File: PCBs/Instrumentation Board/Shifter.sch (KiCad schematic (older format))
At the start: 3 parts, among them U8 PI4ULS5V201TAEX

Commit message: Started instrumentation Netlist
Finished footprints for shifter, regulators and IMUs
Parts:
- U8: footprint (none) -> sot:SOT-23-6; symbol PI4ULS5V201TAEX -> PI4ULS5V201TAEX-RESCUE-instrumentation_board
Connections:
- no-connect marks 2 -> 0
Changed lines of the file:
@@
 EESchema Schematic File Version 2
+LIBS:instrumentation_board-rescue
 LIBS:power
 LIBS:device
@@
 $Descr A4 11693 8268
 encoding utf-8
-Sheet 5 10
+Sheet 7 10
 Title ""
 Date ""
@@
 $EndDescr
 $Comp
-L PI4ULS5V201TAEX U8
+L PI4ULS5V201TAEX-RESCUE-instrumentation_board U8
 U 1 1 5AB871B5
 P 5050 3200
@@
 AR Path="/5AB8D505/5AB871B5" Ref="U13"  Part="1"
 AR Path="/5AB8DDC4/5AB871B5" Ref="U14"  Part="1"
-F 0 "U9" H 5050 3750 60  0000 C CNN
+AR Path="/5AB871B5" Ref="U11"  Part="1"
+F 0 "U11" H 5050 3750 60  0000 C CNN
 F 1 "PI4ULS5V201TAEX" H 5050 2750 60  0000 C CNN
-F 2 "" H 5050 3200 60  0001 C CNN
+F 2 "sot:SOT-23-6" H 5050 3200 60  0001 C CNN
 F 3 "" H 5050 3200 60  0001 C CNN
 	1    5050 3200
@@
 AR Path="/5AB8D505/5AB8720A" Ref="#PWR035"  Part="1"
 AR Path="/5AB8DDC4/5AB8720A" Ref="#PWR038"  Part="1"
-F 0 "#PWR038" H 4500 3050 50  0001 C CNN
+F 0 "#PWR029" H 4500 3050 50  0001 C CNN
 F 1 "GND" H 4500 3150 50  0000 C CNN
 F 2 "" H 4500 3300 50  0001 C CNN
@@
 AR Path="/5AB8D505/5AB87222" Ref="#PWR036"  Part="1"
 AR Path="/5AB8DDC4/5AB87222" Ref="#PWR039"  Part="1"
-F 0 "#PWR039" H 4300 3050 50  0001 C CNN
+F 0 "#PWR030" H 4300 3050 50  0001 C CNN
 F 1 "GND" H 4300 3150 50  0000 C CNN
 F 2 "" H 4300 3300 50  0001 C CNN
@@
 AR Path="/5AB8D505/5AB87230" Ref="#PWR037"  Part="1"
 AR Path="/5AB8DDC4/5AB87230" Ref="#PWR040"  Part="1"
-F 0 "#PWR040" H 5900 3300 50  0001 C CNN
+F 0 "#PWR031" H 5900 3300 50  0001 C CNN
 F 1 "GND" H 5900 3400 50  0000 C CNN
 F 2 "" H 5900 3550 50  0001 C CNN
@@
 AR Path="/5AB8D505/5AB8723F" Ref="C21"  Part="1"
 AR Path="/5AB8DDC4/5AB8723F" Ref="C23"  Part="1"
-F 0 "C13" H 5925 3500 50  0000 L CNN
+F 0 "C17" H 5925 3500 50  0000 L CNN
 F 1 ".1uF" H 5925 3300 50  0000 L CNN
 F 2 "" H 5938 3250 50  0001 C CNN
@@
 AR Path="/5AB8D505/5AB872AC" Ref="C20"  Part="1"
 AR Path="/5AB8DDC4/5AB872AC" Ref="C22"  Part="1"
-F 0 "C12" H 4325 3250 50  0000 L CNN
+F 0 "C16" H 4325 3250 50  0000 L CNN
 F 1 ".1uF" H 4325 3050 50  0000 L CNN
 F 2 "" H 4338 3000 50  0001 C CNN
@@
 Wire Wire Line
 	5900 2850 5900 3250
-NoConn ~ 5500 2950
-NoConn ~ 4600 3050
 Wire Wire Line
 	5500 3150 5900 3150
 Connection ~ 5900 3150
-Text HLabel 5500 3050 2    60   Input ~ 0
+Text HLabel 5500 3000 2    60   Input ~ 0
 B
 Text HLabel 6000 2850 2    60   Input ~ 0
 VccB
 Connection ~ 5900 2850
-Text HLabel 4600 2950 0    60   Input ~ 0
+Text HLabel 4600 3000 0    60   Input ~ 0
 A
 Text HLabel 4200 2850 0    60   Input ~ 0

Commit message: added various review changes
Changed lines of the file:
@@
 $Descr A4 11693 8268
 encoding utf-8
-Sheet 7 10
+Sheet 9 11
 Title ""
 Date ""
@@
 AR Path="/5AB8DDC4/5AB871B5" Ref="U14"  Part="1"
 AR Path="/5AB871B5" Ref="U11"  Part="1"
-F 0 "U11" H 5050 3750 60  0000 C CNN
+F 0 "U14" H 5050 3750 60  0000 C CNN
 F 1 "PI4ULS5V201TAEX" H 5050 2750 60  0000 C CNN
 F 2 "sot:SOT-23-6" H 5050 3200 60  0001 C CNN
@@
 $EndComp
 $Comp
-L GND #PWR020
+L GND #PWR23
 U 1 1 5AB8720A
 P 4500 3300
-AR Path="/5AB87152/5AB8720A" Ref="#PWR020"  Part="1"
-AR Path="/5AB8887F/5AB8720A" Ref="#PWR023"  Part="1"
-AR Path="/5AB899BF/5AB8720A" Ref="#PWR026"  Part="1"
-AR Path="/5AB899C9/5AB8720A" Ref="#PWR029"  Part="1"
-AR Path="/5AB8BB45/5AB8720A" Ref="#PWR032"  Part="1"
-AR Path="/5AB8D505/5AB8720A" Ref="#PWR035"  Part="1"
-AR Path="/5AB8DDC4/5AB8720A" Ref="#PWR038"  Part="1"
-F 0 "#PWR029" H 4500 3050 50  0001 C CNN
+AR Path="/5AB87152/5AB8720A" Ref="#PWR23"  Part="1"
+AR Path="/5AB8887F/5AB8720A" Ref="#PWR26"  Part="1"
+AR Path="/5AB899BF/5AB8720A" Ref="#PWR29"  Part="1"
+AR Path="/5AB899C9/5AB8720A" Ref="#PWR32"  Part="1"
+AR Path="/5AB8BB45/5AB8720A" Ref="#PWR35"  Part="1"
+AR Path="/5AB8D505/5AB8720A" Ref="#PWR38"  Part="1"
+AR Path="/5AB8DDC4/5AB8720A" Ref="#PWR41"  Part="1"
+F 0 "#PWR41" H 4500 3050 50  0001 C CNN
 F 1 "GND" H 4500 3150 50  0000 C CNN
 F 2 "" H 4500 3300 50  0001 C CNN
@@
 	4500 3150 4600 3150
 $Comp
-L GND #PWR021
+L GND #PWR22
 U 1 1 5AB87222
 P 4300 3300
-AR Path="/5AB87152/5AB87222" Ref="#PWR021"  Part="1"
-AR Path="/5AB8887F/5AB87222" Ref="#PWR024"  Part="1"
-AR Path="/5AB899BF/5AB87222" Ref="#PWR027"  Part="1"
-AR Path="/5AB899C9/5AB87222" Ref="#PWR030"  Part="1"
-AR Path="/5AB8BB45/5AB87222" Ref="#PWR033"  Part="1"
-AR Path="/5AB8D505/5AB87222" Ref="#PWR036"  Part="1"
-AR Path="/5AB8DDC4/5AB87222" Ref="#PWR039"  Part="1"
-F 0 "#PWR030" H 4300 3050 50  0001 C CNN
+AR Path="/5AB87152/5AB87222" Ref="#PWR22"  Part="1"
+AR Path="/5AB8887F/5AB87222" Ref="#PWR25"  Part="1"
+AR Path="/5AB899BF/5AB87222" Ref="#PWR28"  Part="1"
+AR Path="/5AB899C9/5AB87222" Ref="#PWR31"  Part="1"
+AR Path="/5AB8BB45/5AB87222" Ref="#PWR34"  Part="1"
+AR Path="/5AB8D505/5AB87222" Ref="#PWR37"  Part="1"
+AR Path="/5AB8DDC4/5AB87222" Ref="#PWR40"  Part="1"
+F 0 "#PWR40" H 4300 3050 50  0001 C CNN
 F 1 "GND" H 4300 3150 50  0000 C CNN
 F 2 "" H 4300 3300 50  0001 C CNN
@@
 $EndComp
 $Comp
-L GND #PWR022
+L GND #PWR24
 U 1 1 5AB87230
 P 5900 3550
-AR Path="/5AB87152/5AB87230" Ref="#PWR022"  Part="1"
-AR Path="/5AB8887F/5AB87230" Ref="#PWR025"  Part="1"
-AR Path="/5AB899BF/5AB87230" Ref="#PWR028"  Part="1"
-AR Path="/5AB899C9/5AB87230" Ref="#PWR031"  Part="1"
-AR Path="/5AB8BB45/5AB87230" Ref="#PWR034"  Part="1"
-AR Path="/5AB8D505/5AB87230" Ref="#PWR037"  Part="1"
-AR Path="/5AB8DDC4/5AB87230" Ref="#PWR040"  Part="1"
-F 0 "#PWR031" H 5900 3300 50  0001 C CNN
+AR Path="/5AB87152/5AB87230" Ref="#PWR24"  Part="1"
+AR Path="/5AB8887F/5AB87230" Ref="#PWR27"  Part="1"
+AR Path="/5AB899BF/5AB87230" Ref="#PWR30"  Part="1"
+AR Path="/5AB899C9/5AB87230" Ref="#PWR33"  Part="1"
+AR Path="/5AB8BB45/5AB87230" Ref="#PWR36"  Part="1"
+AR Path="/5AB8D505/5AB87230" Ref="#PWR39"  Part="1"
+AR Path="/5AB8DDC4/5AB87230" Ref="#PWR42"  Part="1"
+F 0 "#PWR42" H 5900 3300 50  0001 C CNN
 F 1 "GND" H 5900 3400 50  0000 C CNN
 F 2 "" H 5900 3550 50  0001 C CNN
@@
 AR Path="/5AB8D505/5AB8723F" Ref="C21"  Part="1"
 AR Path="/5AB8DDC4/5AB8723F" Ref="C23"  Part="1"
-F 0 "C17" H 5925 3500 50  0000 L CNN
+F 0 "C23" H 5925 3500 50  0000 L CNN
 F 1 ".1uF" H 5925 3300 50  0000 L CNN
 F 2 "" H 5938 3250 50  0001 C CNN
@@
 AR Path="/5AB8D505/5AB872AC" Ref="C20"  Part="1"
 AR Path="/5AB8DDC4/5AB872AC" Ref="C22"  Part="1"
-F 0 "C16" H 4325 3250 50  0000 L CNN
+F 0 "C22" H 4325 3250 50  0000 L CNN
 F 1 ".1uF" H 4325 3050 50  0000 L CNN
 F 2 "" H 4338 3000 50  0001 C CNN

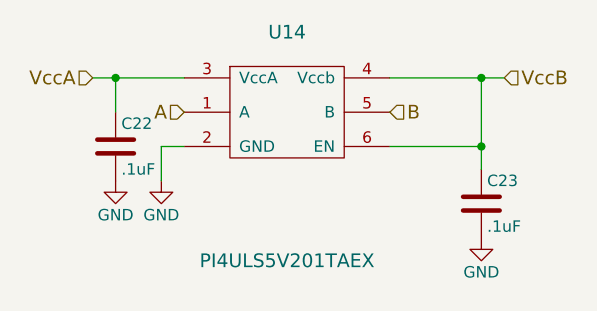
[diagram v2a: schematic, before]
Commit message: swapped TX and RX pins
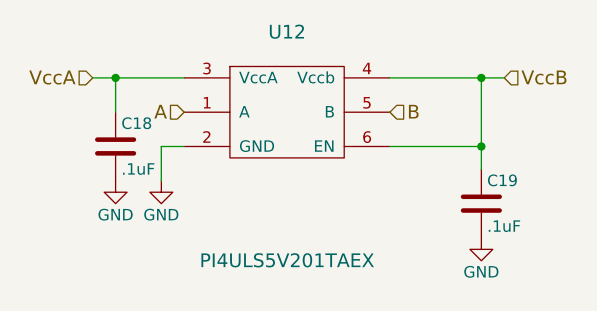
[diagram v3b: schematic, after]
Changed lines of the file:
@@
 $Descr A4 11693 8268
 encoding utf-8
-Sheet 9 11
+Sheet 9 13
 Title ""
 Date ""
@@
 AR Path="/5AB8D505/5AB871B5" Ref="U13"  Part="1"
 AR Path="/5AB8DDC4/5AB871B5" Ref="U14"  Part="1"
-AR Path="/5AB871B5" Ref="U11"  Part="1"
-F 0 "U14" H 5050 3750 60  0000 C CNN
+F 0 "U12" H 5050 3750 60  0000 C CNN
 F 1 "PI4ULS5V201TAEX" H 5050 2750 60  0000 C CNN
 F 2 "sot:SOT-23-6" H 5050 3200 60  0001 C CNN
@@
 AR Path="/5AB8D505/5AB8720A" Ref="#PWR38"  Part="1"
 AR Path="/5AB8DDC4/5AB8720A" Ref="#PWR41"  Part="1"
-F 0 "#PWR41" H 4500 3050 50  0001 C CNN
+F 0 "#PWR35" H 4500 3050 50  0001 C CNN
 F 1 "GND" H 4500 3150 50  0000 C CNN
 F 2 "" H 4500 3300 50  0001 C CNN
@@
 AR Path="/5AB8D505/5AB87222" Ref="#PWR37"  Part="1"
 AR Path="/5AB8DDC4/5AB87222" Ref="#PWR40"  Part="1"
-F 0 "#PWR40" H 4300 3050 50  0001 C CNN
+F 0 "#PWR34" H 4300 3050 50  0001 C CNN
 F 1 "GND" H 4300 3150 50  0000 C CNN
 F 2 "" H 4300 3300 50  0001 C CNN
@@
 AR Path="/5AB8D505/5AB87230" Ref="#PWR39"  Part="1"
 AR Path="/5AB8DDC4/5AB87230" Ref="#PWR42"  Part="1"
-F 0 "#PWR42" H 5900 3300 50  0001 C CNN
+F 0 "#PWR36" H 5900 3300 50  0001 C CNN
 F 1 "GND" H 5900 3400 50  0000 C CNN
 F 2 "" H 5900 3550 50  0001 C CNN
@@
 AR Path="/5AB8D505/5AB8723F" Ref="C21"  Part="1"
 AR Path="/5AB8DDC4/5AB8723F" Ref="C23"  Part="1"
-F 0 "C23" H 5925 3500 50  0000 L CNN
+F 0 "C19" H 5925 3500 50  0000 L CNN
 F 1 ".1uF" H 5925 3300 50  0000 L CNN
 F 2 "" H 5938 3250 50  0001 C CNN
@@
 AR Path="/5AB8D505/5AB872AC" Ref="C20"  Part="1"
 AR Path="/5AB8DDC4/5AB872AC" Ref="C22"  Part="1"
-F 0 "C22" H 4325 3250 50  0000 L CNN
+F 0 "C18" H 4325 3250 50  0000 L CNN
 F 1 ".1uF" H 4325 3050 50  0000 L CNN
 F 2 "" H 4338 3000 50  0001 C CNN
